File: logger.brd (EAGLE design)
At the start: 99 x 44.1 mm, 77 parts, among them IC1 LTC4412, J1 POWER_JACKPTH, Q1 FDN360P, Q2 FDN360P, Q3 2N7002PW, Q4 2N7002PW, U1 DS3231MZ/V+T, U2 FT231X-Q

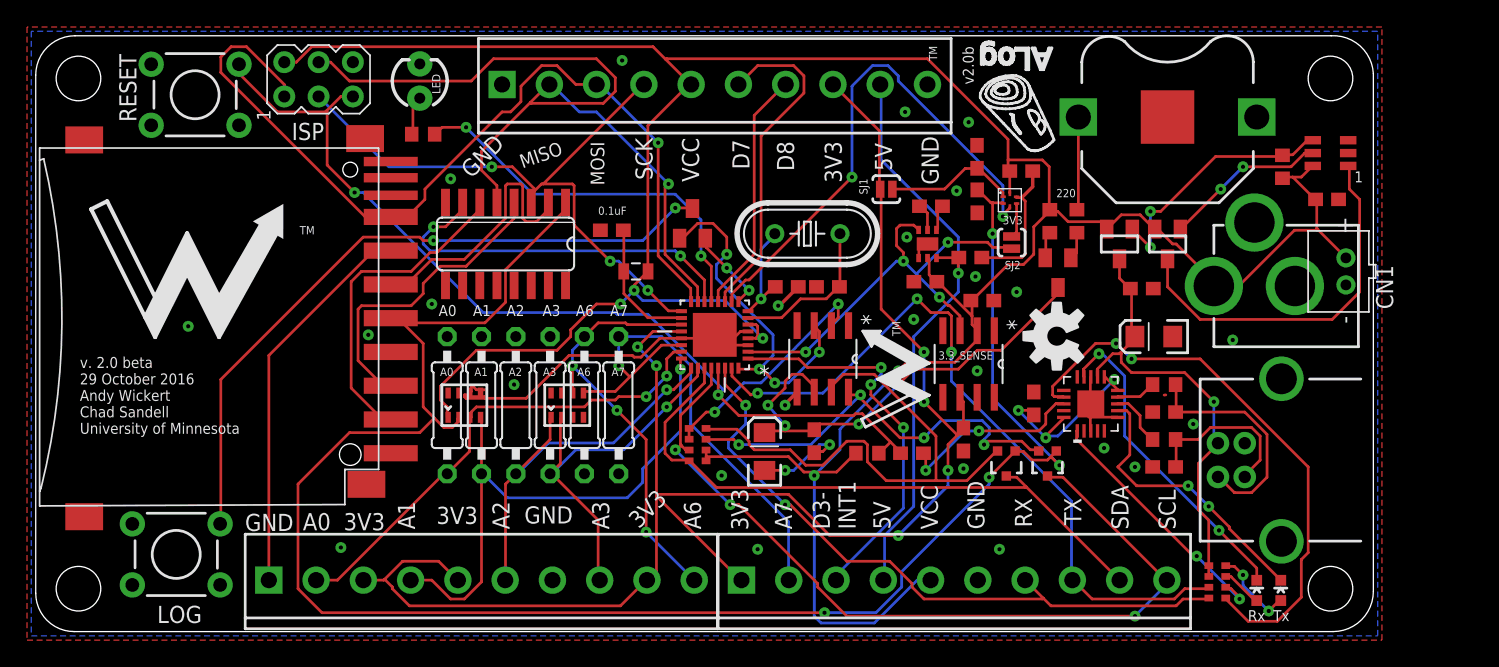
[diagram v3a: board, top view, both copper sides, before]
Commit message: Connected VDD to VCL
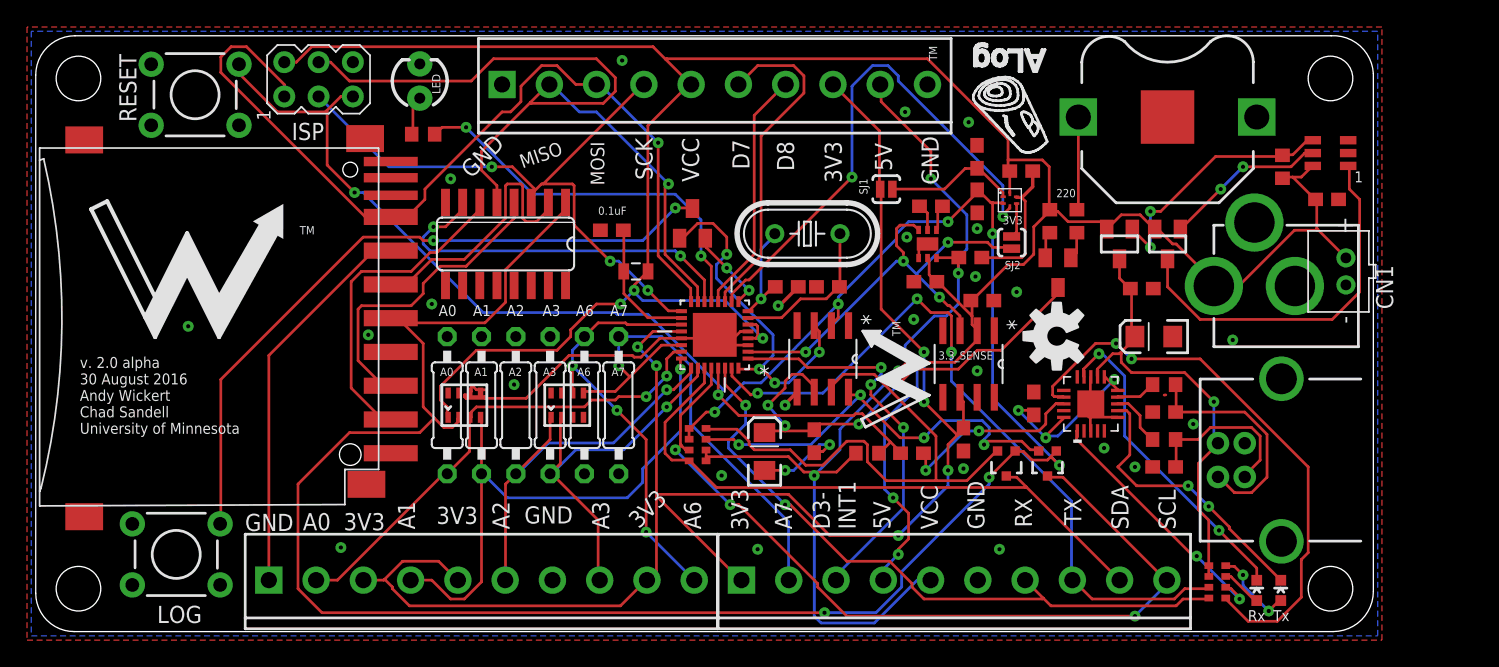
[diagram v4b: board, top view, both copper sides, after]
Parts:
- moved U$2 0.52 mm to (72.1, 38.3)
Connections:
- removed net VCL: RN2.5, RN2.6, U1.2
- net VDD: now also RN2.5, RN2.6, U1.2
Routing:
- net VDD: track 138.0 -> 169.9 mm, vias 4 -> 7
- net VCL: track 17.5 -> 0.00 mm, vias 2 -> 0
- net 5V: track 44.3 -> 47.6 mm, vias 1 -> 4
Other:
- board text added: "v. 2.0 alpha 30 August 2016 Andy Wickert Chad Sandell University of Minnesota"
- board text removed: "v. 2.0 beta 29 October 2016 Andy Wickert Chad Sandell University of Minnesota"
- board text removed: "v2.0b"
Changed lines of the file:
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@@
 <text x="70.2626" y="7.5702" size="1.27" layer="21" rot="R90">GND</text>
 <text x="66.8175" y="7.5702" size="1.27" layer="21" rot="R90">VCC</text>
-<text x="3.2766" y="14.6431" size="0.8128" layer="21">v. 2.0 beta
-29 October 2016
+<text x="3.2766" y="14.6431" size="0.8128" layer="21">v. 2.0 alpha
+30 August 2016
 Andy Wickert
 Chad Sandell
@@
 <text x="38.7802" y="36.3083" size="1.016" layer="21" rot="R199">MISO</text>
 <text x="54.8965" y="36.3083" size="1.27" layer="21" rot="R270">D8</text>
-<text x="69.469" y="40.513" size="0.8128" layer="21" rot="R90">v2.0b</text>
 </plain>
 <attributes>
@@
 </element>
 <element name="JP1" library="SparkFun" package="STAND-OFF" value="STAND-OFF" x="3.175" y="3.175" smashed="yes"/>
-<element name="U$2" library="awickert" package="ALOG_LOGO_V1_SMALL" value="ALOG_LOGO_V1_5.5MM" x="72.592" y="38.469" smashed="yes" rot="R180"/>
+<element name="U$2" library="awickert" package="ALOG_LOGO_V1_SMALL" value="ALOG_LOGO_V1_5.5MM" x="72.084" y="38.342" smashed="yes" rot="R180"/>
 <element name="JP4" library="SparkFun" package="STAND-OFF" value="STAND-OFF" x="3.175" y="40.9575" smashed="yes"/>
 <element name="A1" library="resistor" package="0207/10" value="" x="33.02" y="16.764" smashed="yes" rot="R270">
@@
 <wire x1="69.85" y1="32.639" x2="70.739" y2="31.75" width="0.2032" layer="1"/>
 <wire x1="71.628" y1="31.75" x2="71.643" y2="31.694" width="0.2032" layer="1"/>
-<wire x1="69.85" y1="32.639" x2="69.727" y2="32.706" width="0.2032" layer="1"/>
 <wire x1="73.152" y1="13.335" x2="72.644" y2="13.335" width="0.2032" layer="1"/>
 <wire x1="73.787" y1="12.7" x2="73.152" y2="13.335" width="0.2032" layer="1"/>
@@
 <via x="70.612" y="11.43" extent="1-16" drill="0.3048"/>
 <via x="58.42" y="1.397" extent="1-16" drill="0.3048"/>
+<contactref element="RN2" pad="5"/>
+<contactref element="RN2" pad="6"/>
+<contactref element="U1" pad="2"/>
+<wire x1="49.657" y1="16.256" x2="48.514" y2="15.113" width="0.2032" layer="1"/>
+<wire x1="50.292" y1="16.256" x2="49.657" y2="16.256" width="0.2032" layer="1"/>
+<wire x1="59.436" y1="24.257" x2="53.721" y2="18.415" width="0.2032" layer="16"/>
+<wire x1="53.721" y1="18.415" x2="52.451" y2="18.415" width="0.2032" layer="16"/>
+<wire x1="52.451" y1="18.415" x2="50.292" y2="16.256" width="0.2032" layer="16"/>
+<wire x1="59.436" y1="23.241" x2="59.436" y2="24.257" width="0.2032" layer="1"/>
+<wire x1="58.928" y1="22.733" x2="59.436" y2="23.241" width="0.2032" layer="1"/>
+<wire x1="58.928" y1="22.733" x2="58.928" y2="22.6568" width="0.2032" layer="1"/>
+<via x="50.292" y="16.256" extent="1-16" drill="0.3048"/>
+<via x="59.436" y="24.257" extent="1-16" drill="0.3048"/>
+<wire x1="48.387" y1="14.986" x2="48.387" y2="14.351" width="0.2032" layer="1"/>
+<wire x1="48.387" y1="14.351" x2="48.397" y2="14.243" width="0.2032" layer="1"/>
+<wire x1="48.387" y1="14.986" x2="48.397" y2="15.043" width="0.2032" layer="1"/>
+<wire x1="48.514" y1="15.113" x2="48.397" y2="15.043" width="0.2032" layer="1"/>
+<wire x1="59.436" y1="24.765" x2="59.436" y2="24.257" width="0.2032" layer="16"/>
+<wire x1="63.754" y1="29.083" x2="59.436" y2="24.765" width="0.2032" layer="16"/>
+<wire x1="63.754" y1="29.464" x2="63.754" y2="29.083" width="0.2032" layer="16"/>
+<wire x1="64.643" y1="30.353" x2="63.754" y2="29.464" width="0.2032" layer="16"/>
+<wire x1="67.564" y1="30.353" x2="64.643" y2="30.353" width="0.2032" layer="16"/>
+<wire x1="69.85" y1="32.639" x2="67.564" y2="30.353" width="0.2032" layer="1"/>
+<wire x1="69.85" y1="32.639" x2="69.727" y2="32.706" width="0.2032" layer="1"/>
+<via x="67.564" y="30.353" extent="1-16" drill="0.3048"/>
 </signal>
 <signal name="LED+">
@@
 <via x="47.371" y="31.369" extent="1-16" drill="0.3048"/>
 <via x="29.464" y="28.956" extent="1-16" drill="0.3048"/>
-</signal>
-<signal name="VCL">
-<contactref element="RN2" pad="6"/>
-<contactref element="RN2" pad="5"/>
-<contactref element="U1" pad="2"/>
-<wire x1="48.387" y1="14.986" x2="48.387" y2="14.351" width="0.2032" layer="1"/>
-<wire x1="48.387" y1="14.351" x2="48.397" y2="14.243" width="0.2032" layer="1"/>
-<wire x1="48.387" y1="14.986" x2="48.397" y2="15.043" width="0.2032" layer="1"/>
-<wire x1="49.657" y1="16.256" x2="48.514" y2="15.113" width="0.2032" layer="1"/>
-<wire x1="50.292" y1="16.256" x2="49.657" y2="16.256" width="0.2032" layer="1"/>
-<wire x1="59.436" y1="24.257" x2="53.721" y2="18.415" width="0.2032" layer="16"/>
-<wire x1="53.721" y1="18.415" x2="52.451" y2="18.415" width="0.2032" layer="16"/>
-<wire x1="52.451" y1="18.415" x2="50.292" y2="16.256" width="0.2032" layer="16"/>
-<wire x1="59.436" y1="23.241" x2="59.436" y2="24.257" width="0.2032" layer="1"/>
-<wire x1="58.928" y1="22.733" x2="59.436" y2="23.241" width="0.2032" layer="1"/>
-<wire x1="48.514" y1="15.113" x2="48.397" y2="15.043" width="0.2032" layer="1"/>
-<wire x1="58.928" y1="22.733" x2="58.928" y2="22.6568" width="0.2032" layer="1"/>
-<via x="50.292" y="16.256" extent="1-16" drill="0.3048"/>
-<via x="59.436" y="24.257" extent="1-16" drill="0.3048"/>
 </signal>
 <signal name="GND">
@@
 <wire x1="78.105" y1="15.875" x2="78.137" y2="16.859" width="0.2032" layer="1"/>
 <wire x1="80.137" y1="15.875" x2="80.137" y2="15.859" width="0.2032" layer="1"/>
-<via x="68.199" y="32.639" extent="1-16" drill="0.3048" shape="octagon"/>
 <via x="69.596" y="26.289" extent="1-16" drill="0.3048" shape="octagon"/>
 <wire x1="65.3876" y1="27.6606" x2="65.405" y2="27.6606" width="0.2032" layer="1"/>
@@
 <via x="35.433" y="18.288" extent="1-16" drill="0.3048" shape="octagon"/>
 <via x="11.303" y="22.606" extent="1-16" drill="0.3048" shape="octagon"/>
+<via x="69.723" y="29.845" extent="1-16" drill="0.3048" shape="octagon"/>
 </signal>
 <signal name="5V">
@@
 <wire x1="66.802" y1="27.686" x2="66.7084" y2="27.6606" width="0.2032" layer="1"/>
 <wire x1="68.326" y1="26.543" x2="68.326" y2="27.686" width="0.2032" layer="1"/>
-<wire x1="68.326" y1="29.21" x2="68.326" y2="26.543" width="0.2032" layer="16"/>
-<wire x1="62.611" y1="34.925" x2="68.326" y2="29.21" width="0.2032" layer="16"/>
-<wire x1="62.611" y1="40.513" x2="62.611" y2="34.925" width="0.2032" layer="16"/>
+<wire x1="68.326" y1="27.686" x2="68.326" y2="26.543" width="0.2032" layer="16"/>
+<wire x1="68.961" y1="28.321" x2="68.326" y2="27.686" width="0.2032" layer="16"/>
+<wire x1="68.961" y1="30.861" x2="68.961" y2="28.321" width="0.2032" layer="16"/>
+<wire x1="66.294" y1="33.528" x2="68.961" y2="30.861" width="0.2032" layer="16"/>
+<wire x1="66.294" y1="35.56" x2="66.294" y2="33.528" width="0.2032" layer="1"/>
+<wire x1="62.611" y1="39.243" x2="66.294" y2="35.56" width="0.2032" layer="1"/>
+<wire x1="62.611" y1="40.513" x2="62.611" y2="39.243" width="0.2032" layer="1"/>
 <wire x1="68.326" y1="27.686" x2="68.365" y2="27.697" width="0.2032" layer="1"/>
-<wire x1="62.611" y1="40.513" x2="62.544" y2="40.513" width="0.2032" layer="16"/>
-<wire x1="62.865" y1="7.112" x2="62.865" y2="3.81" width="0.2032" layer="16"/>
-<wire x1="65.024" y1="9.271" x2="62.865" y2="7.112" width="0.2032" layer="16"/>
-<wire x1="65.024" y1="21.844" x2="65.024" y2="9.271" width="0.2032" layer="16"/>
-<wire x1="68.326" y1="25.146" x2="65.024" y2="21.844" width="0.2032" layer="16"/>
-<wire x1="68.326" y1="26.543" x2="68.326" y2="25.146" width="0.2032" layer="16"/>
+<wire x1="62.611" y1="40.513" x2="62.544" y2="40.513" width="0.2032" layer="1"/>
+<wire x1="62.865" y1="4.699" x2="62.865" y2="3.81" width="0.2032" layer="16"/>
+<wire x1="63.881" y1="5.715" x2="62.865" y2="4.699" width="0.2032" layer="16"/>
+<wire x1="63.881" y1="6.096" x2="63.881" y2="5.715" width="0.2032" layer="1"/>
+<wire x1="64.643" y1="6.858" x2="63.881" y2="6.096" width="0.2032" layer="1"/>
+<wire x1="64.643" y1="8.763" x2="64.643" y2="6.858" width="0.2032" layer="1"/>
+<wire x1="63.5" y1="9.906" x2="64.643" y2="8.763" width="0.2032" layer="1"/>
+<wire x1="62.865" y1="10.541" x2="63.5" y2="9.906" width="0.2032" layer="16"/>
+<wire x1="62.865" y1="15.621" x2="62.865" y2="10.541" width="0.2032" layer="16"/>
+<wire x1="65.278" y1="18.034" x2="62.865" y2="15.621" width="0.2032" layer="16"/>
+<wire x1="65.278" y1="19.812" x2="65.278" y2="18.034" width="0.2032" layer="16"/>
+<wire x1="64.389" y1="20.701" x2="65.278" y2="19.812" width="0.2032" layer="16"/>
+<wire x1="64.389" y1="21.209" x2="64.389" y2="20.701" width="0.2032" layer="16"/>
+<wire x1="66.548" y1="23.368" x2="64.389" y2="21.209" width="0.2032" layer="16"/>
+<wire x1="67.437" y1="23.368" x2="66.548" y2="23.368" width="0.2032" layer="16"/>
+<wire x1="68.326" y1="24.257" x2="67.437" y2="23.368" width="0.2032" layer="16"/>
+<wire x1="68.326" y1="26.543" x2="68.326" y2="24.257" width="0.2032" layer="16"/>
 <wire x1="62.865" y1="3.81" x2="62.772" y2="3.81" width="0.2032" layer="16"/>
 <via x="68.326" y="26.543" extent="1-16" drill="0.3048"/>
+<via x="66.294" y="33.528" extent="1-16" drill="0.3048"/>
+<via x="63.881" y="5.715" extent="1-16" drill="0.3048"/>
+<via x="63.5" y="9.906" extent="1-16" drill="0.3048"/>
 </signal>
 <signal name="D4-SENSE_LDO_SWITCH">

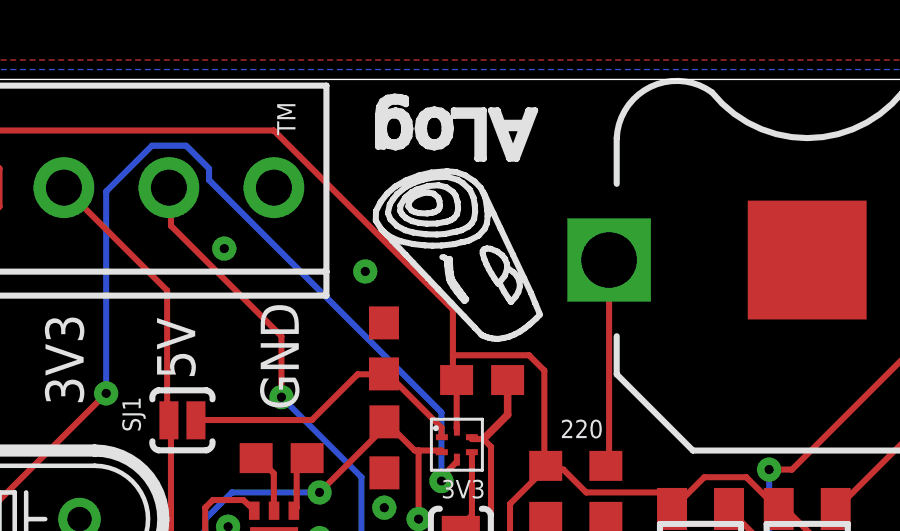
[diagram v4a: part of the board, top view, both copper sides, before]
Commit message: Version number visible
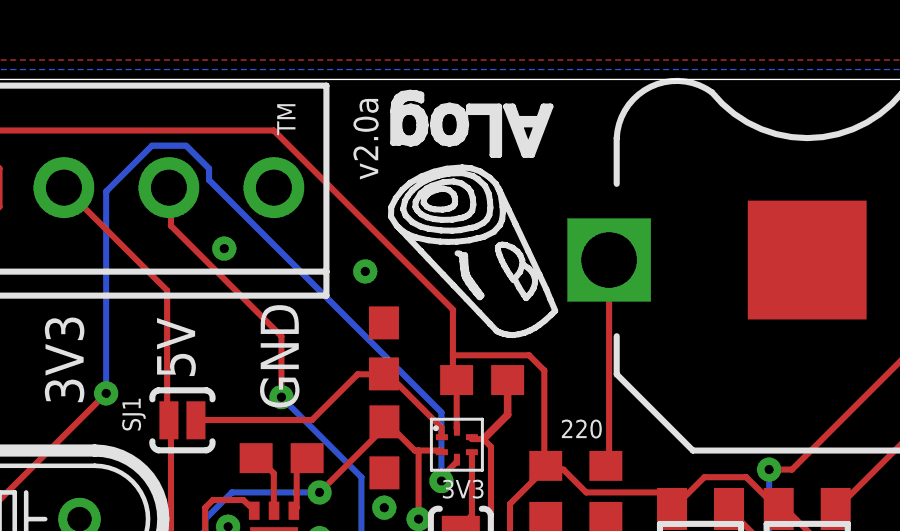
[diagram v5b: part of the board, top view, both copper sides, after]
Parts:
- moved U$2 0.52 mm to (72.6, 38.5)
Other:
- board text added: "v2.0a"
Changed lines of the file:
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@@
 <text x="38.7802" y="36.3083" size="1.016" layer="21" rot="R199">MISO</text>
 <text x="54.8965" y="36.3083" size="1.27" layer="21" rot="R270">D8</text>
+<text x="68.707" y="43.561" size="0.8128" layer="21" rot="R270">v2.0a</text>
 </plain>
 <attributes>
@@
 </element>
 <element name="JP1" library="SparkFun" package="STAND-OFF" value="STAND-OFF" x="3.175" y="3.175" smashed="yes"/>
-<element name="U$2" library="awickert" package="ALOG_LOGO_V1_SMALL" value="ALOG_LOGO_V1_5.5MM" x="72.084" y="38.342" smashed="yes" rot="R180"/>
+<element name="U$2" library="awickert" package="ALOG_LOGO_V1_SMALL" value="ALOG_LOGO_V1_5.5MM" x="72.592" y="38.469" smashed="yes" rot="R180"/>
 <element name="JP4" library="SparkFun" package="STAND-OFF" value="STAND-OFF" x="3.175" y="40.9575" smashed="yes"/>
 <element name="A1" library="resistor" package="0207/10" value="" x="33.02" y="16.764" smashed="yes" rot="R270">
